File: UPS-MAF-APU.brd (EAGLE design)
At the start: 65 x 30 mm, 3 parts, among them J1 CONNECTOR_PI_40_PIN, J3 CONNECTOR_4, U1 OLED_I2C

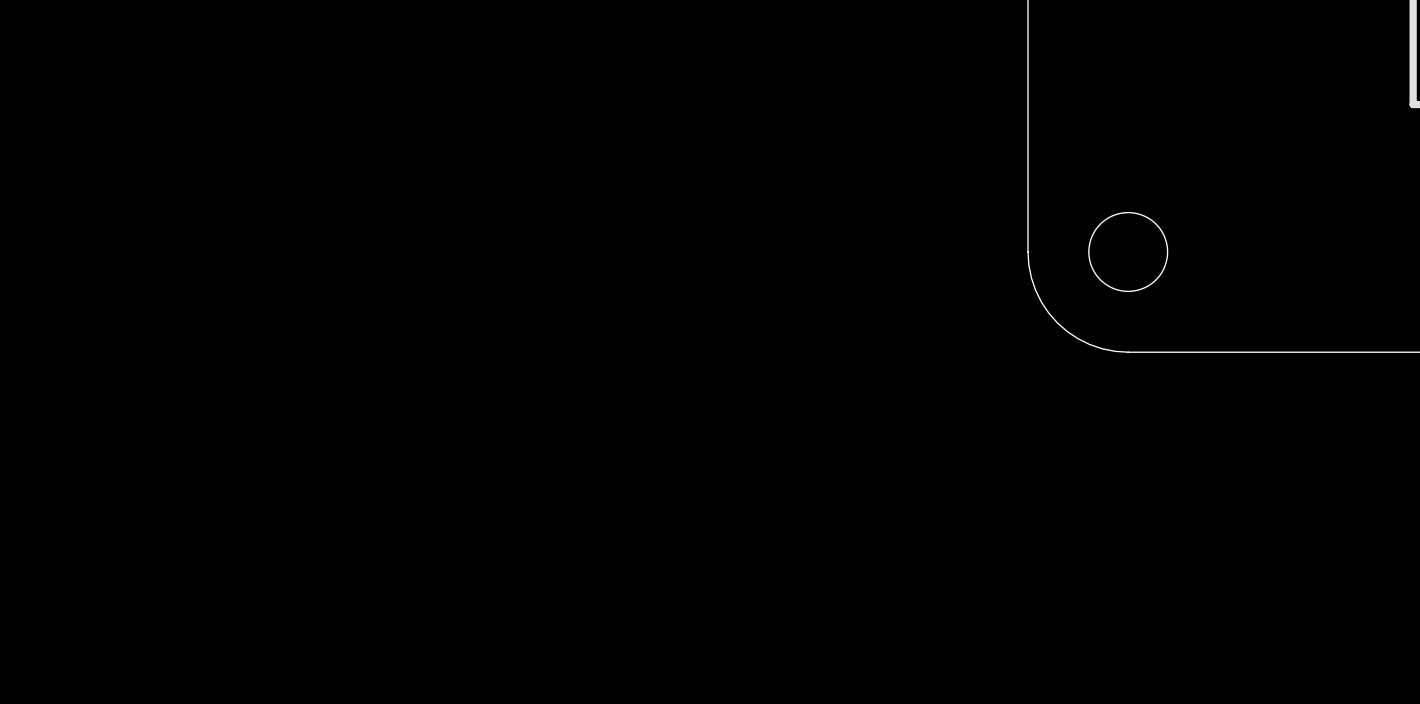
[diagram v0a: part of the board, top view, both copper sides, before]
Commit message: Add parts to library, Schematic. Add barrel power jack, INA260 I/V sensor, 5V Murata SMPS.  Change parts to UPS library.
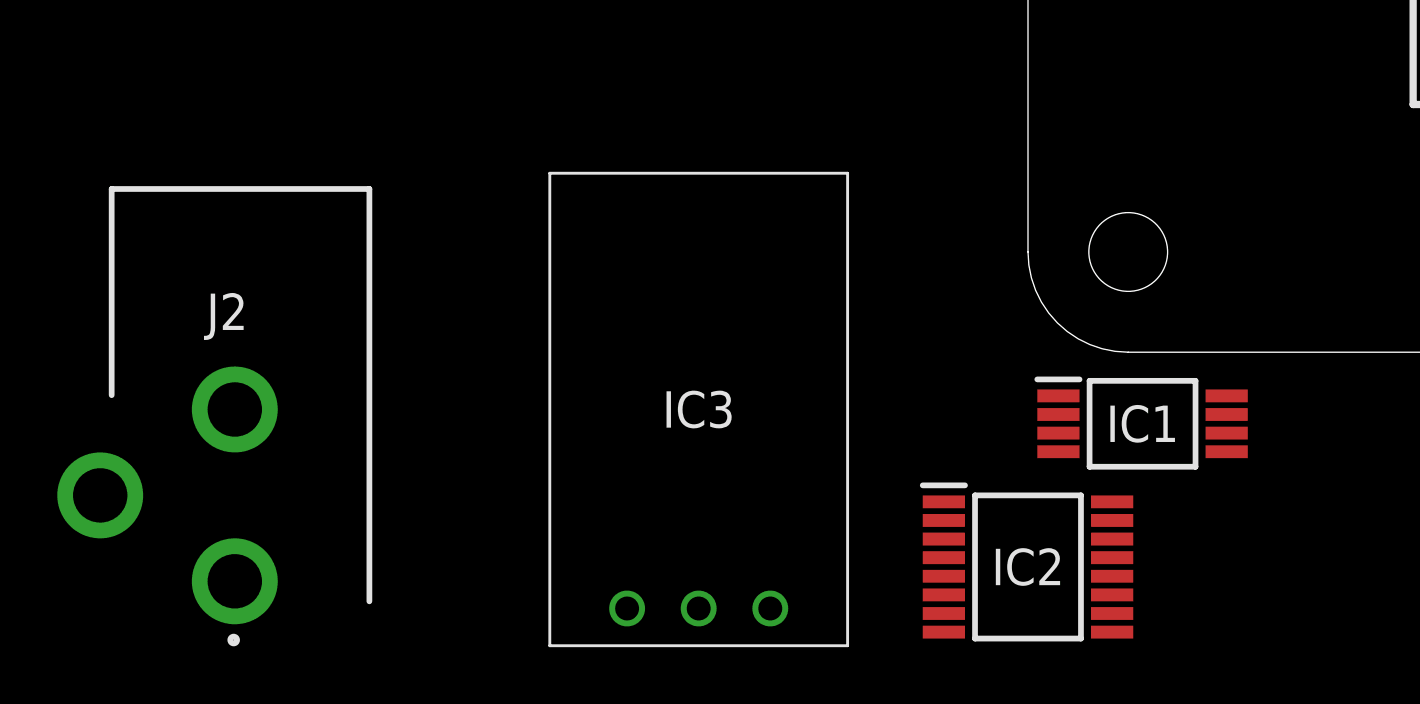
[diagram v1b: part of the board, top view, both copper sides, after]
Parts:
- added IC1: M24C32-RDW6TP, APU_ENGR480_UPS_EAGLE_Library:SOP65P640X120-8N
- added IC2: INA260AIPW, APU_ENGR480_UPS_EAGLE_Library:SOP65P640X120-16N
- added IC3: OKI-78SR-5_1.5-W36H-C, APU_ENGR480_UPS_EAGLE_Library:OKI-78SR-HORIZONTAL
- added J2: PJ-102AH, APU_ENGR480_UPS_EAGLE_Library:PJ-102AH
- J1: device ConnectBox_2019:2X20 -> APU_ENGR480_UPS_EAGLE_Library:2X20
- J3: device ConnectBox_2019:ESQ-104-XX-X-S -> APU_ENGR480_UPS_EAGLE_Library:ESQ-104-XX-X-S
- U1: device ConnectBox_2019:OLED-I2C -> APU_ENGR480_UPS_EAGLE_Library:OLED-I2C
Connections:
- new net GND_1: IC2.6
- new net GND_2: IC2.11
- new net VBUS: IC2.12
- new net VS: IC2.10
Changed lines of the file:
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@@
 </autorouter>
 <elements>
-<element name="J1" library="ConnectBox_2019" package="2X20" value="CONNECTOR_PI_40_PIN" x="32.5" y="26.5" smashed="yes">
+<element name="J1" library="APU_ENGR480_UPS_EAGLE_Library" package="2X20" value="CONNECTOR_PI_40_PIN" x="32.5" y="26.5" smashed="yes">
 <attribute name="NAME" x="7.1" y="29.675" size="1.27" layer="25" ratio="10"/>
 <attribute name="VALUE" x="7.1" y="22.055" size="1.27" layer="27"/>
 </element>
-<element name="U1" library="ConnectBox_2019" package="OLED-I2C" value="OLED_I2C" x="32.5" y="15" smashed="yes" rot="R180">
+<element name="U1" library="APU_ENGR480_UPS_EAGLE_Library" package="OLED-I2C" value="OLED_I2C" x="32.5" y="15" smashed="yes" rot="R180">
 <attribute name="NAME" x="32.5" y="15.5" size="1.524" layer="25" font="vector" ratio="10" align="center"/>
 <attribute name="NAME" x="32.5" y="15" size="2.54" layer="51" ratio="10" rot="R270" align="center"/>
 </element>
-<element name="J3" library="ConnectBox_2019" package="ESQ-104-XX-X-S" value="CONNECTOR_4" x="50.28" y="15" smashed="yes" rot="R270">
+<element name="J3" library="APU_ENGR480_UPS_EAGLE_Library" package="ESQ-104-XX-X-S" value="CONNECTOR_4" x="50.28" y="15" smashed="yes" rot="R270">
 <attribute name="NAME" x="53.455" y="15" size="1.524" layer="25" font="vector" ratio="10" rot="R270" align="center"/>
 <attribute name="NAME" x="50.28" y="15" size="1.524" layer="51" ratio="10" rot="R270" align="center"/>
 <attribute name="VALUE" x="47.105" y="15" size="1.524" layer="27" font="vector" ratio="10" rot="R270" align="center"/>
+</element>
+<element name="IC1" library="APU_ENGR480_UPS_EAGLE_Library" package="SOP65P640X120-8N" value="M24C32-RDW6TP" x="4" y="-2.5" smashed="yes">
+<attribute name="DESCRIPTION" value="STMICROELECTRONICS - M24C32-RDW6TP - EEPROM, 32KBIT, I2C, 1MHZ, TSSOP-8" x="4" y="-2.5" size="1.778" layer="27" display="off"/>
+<attribute name="HEIGHT" value="1.2mm" x="4" y="-2.5" size="1.778" layer="27" display="off"/>
+<attribute name="MANUFACTURER_NAME" value="STMicroelectronics" x="4" y="-2.5" size="1.778" layer="27" display="off"/>
+<attribute name="MANUFACTURER_PART_NUMBER" value="M24C32-RDW6TP" x="4" y="-2.5" size="1.778" layer="27" display="off"/>
+<attribute name="MOUSER_PART_NUMBER" value="511-M24C32-RDW6TP" x="4" y="-2.5" size="1.778" layer="27" display="off"/>
+<attribute name="MOUSER_PRICE-STOCK" value="https://www.mouser.com/Search/Refine.aspx?Keyword=511-M24C32-RDW6TP" x="4" y="-2.5" size="1.778" layer="27" display="off"/>
+<attribute name="NAME" x="4" y="-2.5" size="1.27" layer="25" align="center"/>
+<attribute name="RS_PART_NUMBER" value="" x="4" y="-2.5" size="1.778" layer="27" display="off"/>
+<attribute name="RS_PRICE-STOCK" value="" x="4" y="-2.5" size="1.778" layer="27" display="off"/>
+<attribute name="VALUE" x="4" y="-2.5" size="1.27" layer="27" align="center"/>
+</element>
+<element name="IC2" library="APU_ENGR480_UPS_EAGLE_Library" package="SOP65P640X120-16N" value="INA260AIPW" x="0" y="-7.5" smashed="yes">
+<attribute name="DESCRIPTION" value="36V, Bi-Dir, High Accuracy, Low-/High-Side, I2C Current/Pwr Monitor w/Integrated 2m Shunt Resistor" x="0" y="-7.5" size="1.778" layer="27" display="off"/>
+<attribute name="HEIGHT" value="1.2mm" x="0" y="-7.5" size="1.778" layer="27" display="off"/>
+<attribute name="MANUFACTURER_NAME" value="Texas Instruments" x="0" y="-7.5" size="1.778" layer="27" display="off"/>
+<attribute name="MANUFACTURER_PART_NUMBER" value="INA260AIPW" x="0" y="-7.5" size="1.778" layer="27" display="off"/>
+<attribute name="MOUSER_PART_NUMBER" value="595-INA260AIPW" x="0" y="-7.5" size="1.778" layer="27" display="off"/>
+<attribute name="MOUSER_PRICE-STOCK" value="https://www.mouser.com/Search/Refine.aspx?Keyword=595-INA260AIPW" x="0" y="-7.5" size="1.778" layer="27" display="off"/>
+<attribute name="NAME" x="0" y="-7.5" size="1.27" layer="25" align="center"/>
+<attribute name="RS_PART_NUMBER" value="" x="0" y="-7.5" size="1.778" layer="27" display="off"/>
+<attribute name="RS_PRICE-STOCK" value="" x="0" y="-7.5" size="1.778" layer="27" display="off"/>
+<attribute name="VALUE" x="0" y="-7.5" size="1.27" layer="27" align="center"/>
+</element>
+<element name="IC3" library="APU_ENGR480_UPS_EAGLE_Library" package="OKI-78SR-HORIZONTAL" value="OKI-78SR-5_1.5-W36H-C" x="-11.5" y="-2" smashed="yes">
+<attribute name="DESCRIPTION" value="Switching Regulator 7-36Vin 5Vo 1.5A Non-Isolated DC-DC Converter, 5V dc Output, 1.5A" x="-11.5" y="-2" size="1.778" layer="27" display="off"/>
+<attribute name="HEIGHT" value="mm" x="-11.5" y="-2" size="1.778" layer="27" display="off"/>
+<attribute name="MANUFACTURER_NAME" value="Murata Electronics" x="-11.5" y="-2" size="1.778" layer="27" display="off"/>
+<attribute name="MANUFACTURER_PART_NUMBER" value="OKI-78SR-5/1.5-W36H-C" x="-11.5" y="-2" size="1.778" layer="27" display="off"/>
+<attribute name="MOUSER_PART_NUMBER" value="580-OKI78SR51.5W36HC" x="-11.5" y="-2" size="1.778" layer="27" display="off"/>
+<attribute name="MOUSER_PRICE-STOCK" value="https://www.mouser.com/Search/Refine.aspx?Keyword=580-OKI78SR51.5W36HC" x="-11.5" y="-2" size="1.778" layer="27" display="off"/>
+<attribute name="NAME" x="-11.5" y="-2" size="1.27" layer="25" align="center"/>
+<attribute name="RS_PART_NUMBER" value="1736931" x="-11.5" y="-2" size="1.778" layer="27" display="off"/>
+<attribute name="RS_PRICE-STOCK" value="http://uk.rs-online.com/web/p/products/1736931" x="-11.5" y="-2" size="1.778" layer="27" display="off"/>
+<attribute name="VALUE" x="-11.5" y="-2" size="1.27" layer="27" align="center"/>
+</element>
+<element name="J2" library="APU_ENGR480_UPS_EAGLE_Library" package="PJ-102AH" value="PJ-102AH" x="-32" y="-5" smashed="yes">
+<attribute name="DESCRIPTION" value="DC POWER JACK" x="-32" y="-5" size="1.778" layer="27" display="off"/>
+<attribute name="HEIGHT" value="mm" x="-32" y="-5" size="1.778" layer="27" display="off"/>
+<attribute name="MANUFACTURER_NAME" value="CUI" x="-32" y="-5" size="1.778" layer="27" display="off"/>
+<attribute name="MANUFACTURER_PART_NUMBER" value="PJ-102AH" x="-32" y="-5" size="1.778" layer="27" display="off"/>
+<attribute name="MOUSER_PART_NUMBER" value="490-PJ-102AH" x="-32" y="-5" size="1.778" layer="27" display="off"/>
+<attribute name="MOUSER_PRICE-STOCK" value="https://www.mouser.com/Search/Refine.aspx?Keyword=490-PJ-102AH" x="-32" y="-5" size="1.778" layer="27" display="off"/>
+<attribute name="NAME" x="-27.965" y="1.411" size="1.27" layer="25" align="center"/>
+<attribute name="RS_PART_NUMBER" value="" x="-32" y="-5" size="1.778" layer="27" display="off"/>
+<attribute name="RS_PRICE-STOCK" value="" x="-32" y="-5" size="1.778" layer="27" display="off"/>
+<attribute name="VALUE" x="-27.965" y="1.411" size="1.27" layer="27" align="center"/>
 </element>
 </elements>
@@
 <wire x1="10.91" y1="25.23" x2="50.28" y2="11.19" width="0" layer="19" extent="1-1"/>
 </signal>
+<signal name="GND_1">
+<contactref element="IC2" pad="6"/>
+</signal>
+<signal name="VBUS">
+<contactref element="IC2" pad="12"/>
+</signal>
+<signal name="GND_2">
+<contactref element="IC2" pad="11"/>
+</signal>
+<signal name="VS">
+<contactref element="IC2" pad="10"/>
+</signal>
 </signals>

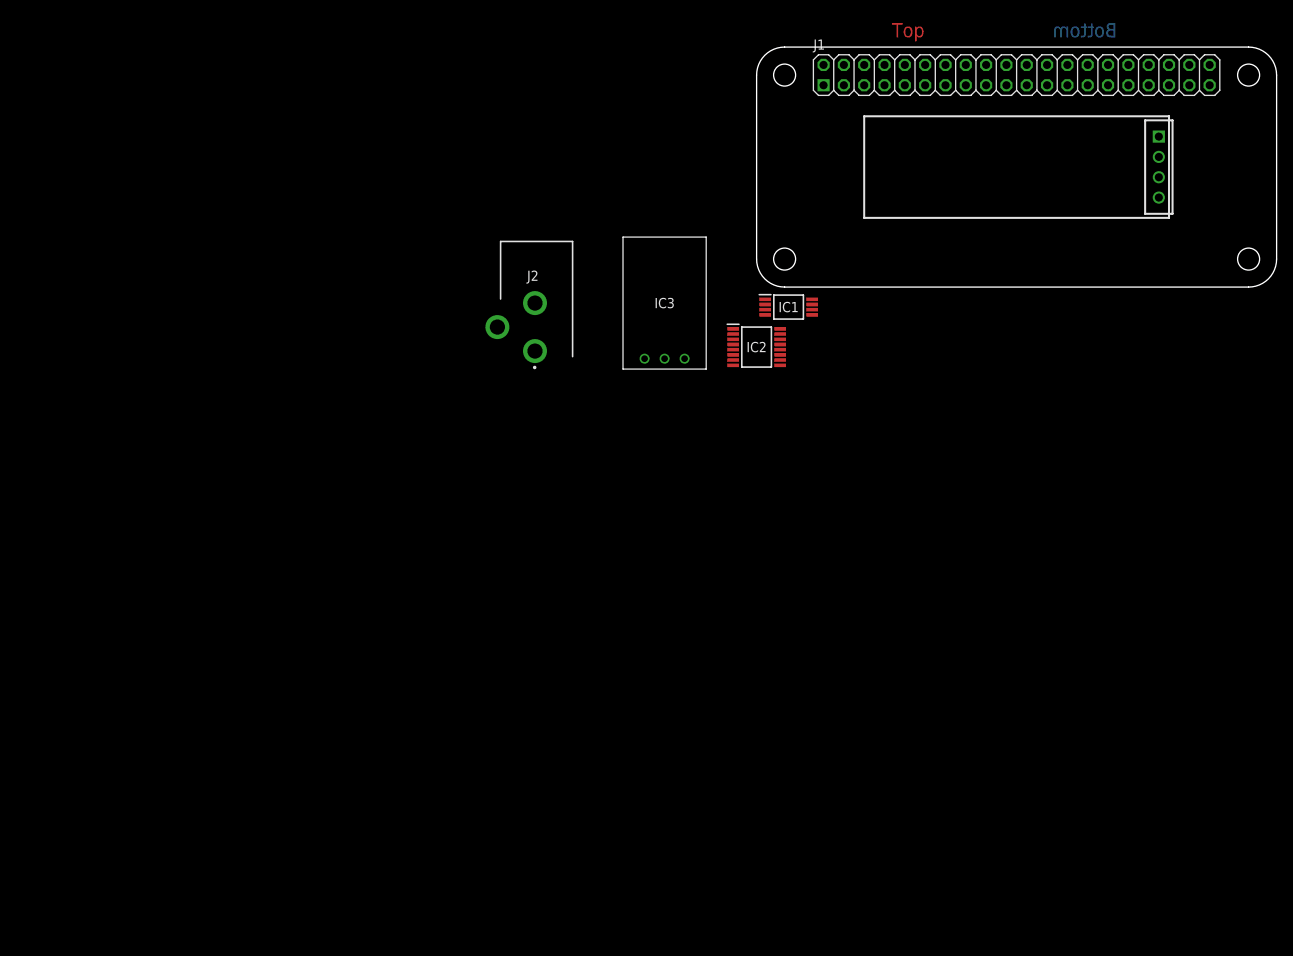
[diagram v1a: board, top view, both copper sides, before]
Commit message: Add tons of parts to Library and Schematic, update symbol styles.
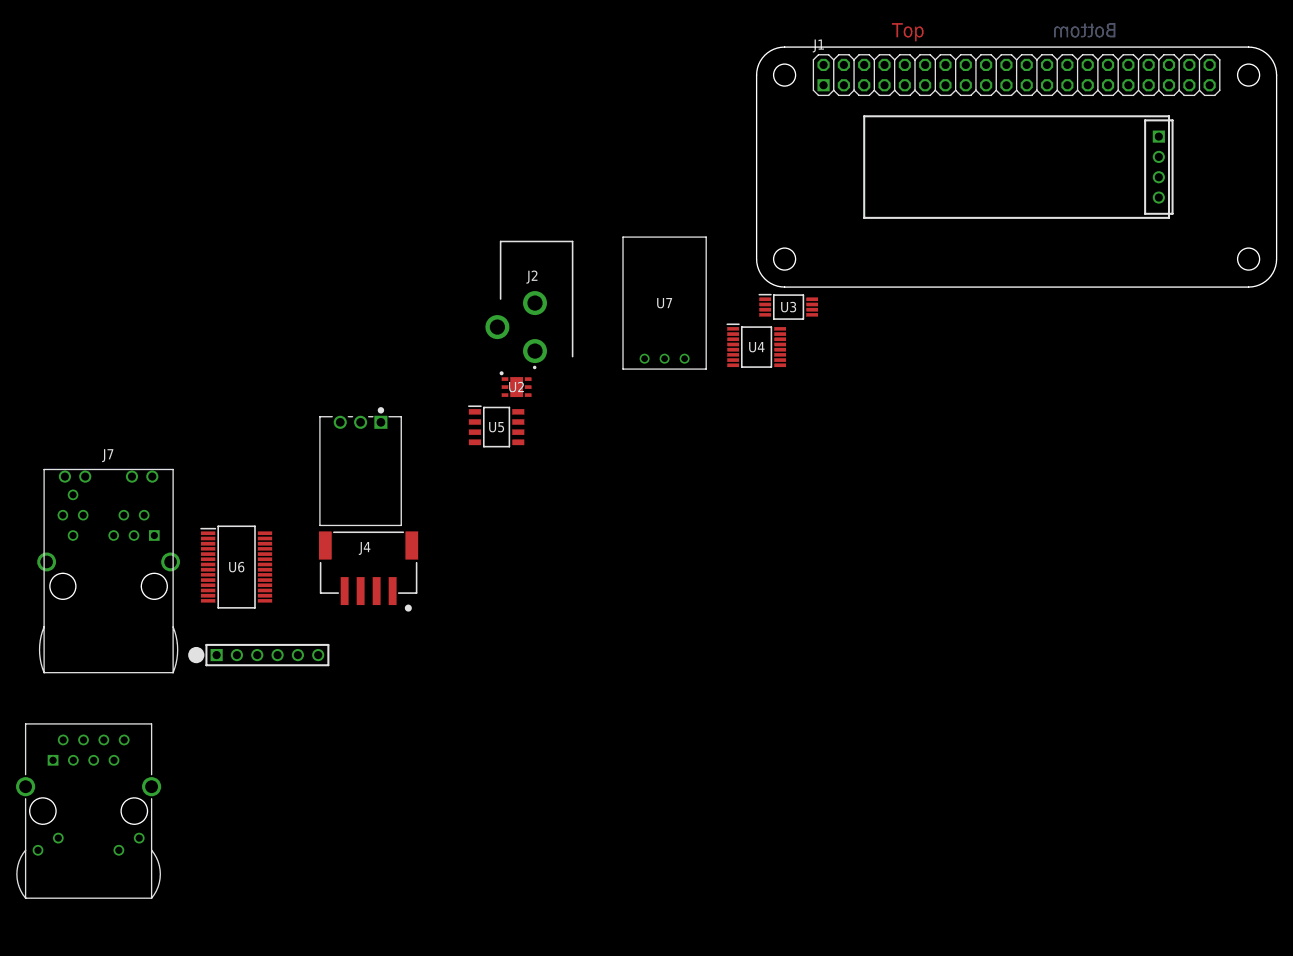
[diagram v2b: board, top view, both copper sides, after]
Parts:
- added J4: S4B-PH-SM4-TB(LF)(SN), APU_ENGR480_UPS_EAGLE_Library:S4B-PH-SM4-TB
- added J5: CONNECTOR-3, APU_ENGR480_UPS_EAGLE_Library:MOLEX_70553-0002
- added J6: CONNECTOR-6-FTDI, APU_ENGR480_UPS_EAGLE_Library:ESQ-106-XX-X-S
- added J7: BEL_STEWART_SI-52003-F_MAGJACK, APU_ENGR480_UPS_EAGLE_Library:BEL_STEWART_SI-52003-F_MAGJACK
- added J8: RB1-125BAG1A, APU_ENGR480_UPS_EAGLE_Library:WIZNET_RB1-125BAG1A
- added U2: SI7006-A20-IM, APU_ENGR480_UPS_EAGLE_Library:SON100P300X300X80-7N
- added U5: SI8621AB-B-ISR, APU_ENGR480_UPS_EAGLE_Library:SOIC127P600X175-8N
- added U6: ENC28J60_SS, APU_ENGR480_UPS_EAGLE_Library:SOP65P780X200-28N
- renumbered IC1 to U3, IC2 to U4, IC3 to U7
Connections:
- net +3V3 renamed 3.3V
- new net PAD: U2.7
- new net VDD: U2.5, U6.28
- new net VDDOSC: U6.25
- new net VDDPLL: U6.20
- new net VDDRX: U6.19
- new net VDDTX: U6.15
- new net VSS: U6.2
- new net VSSOSC: U6.22
- new net VSSPLL: U6.21
- new net VSSRX: U6.11
- new net VSSTX: U6.18
- net GND: now also U2.2
